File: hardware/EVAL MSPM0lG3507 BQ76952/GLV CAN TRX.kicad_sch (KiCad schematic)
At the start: 11 parts, among them U10 MCP2542FDxMF, U5 ISO7721D, U8 L78L05_SOT89

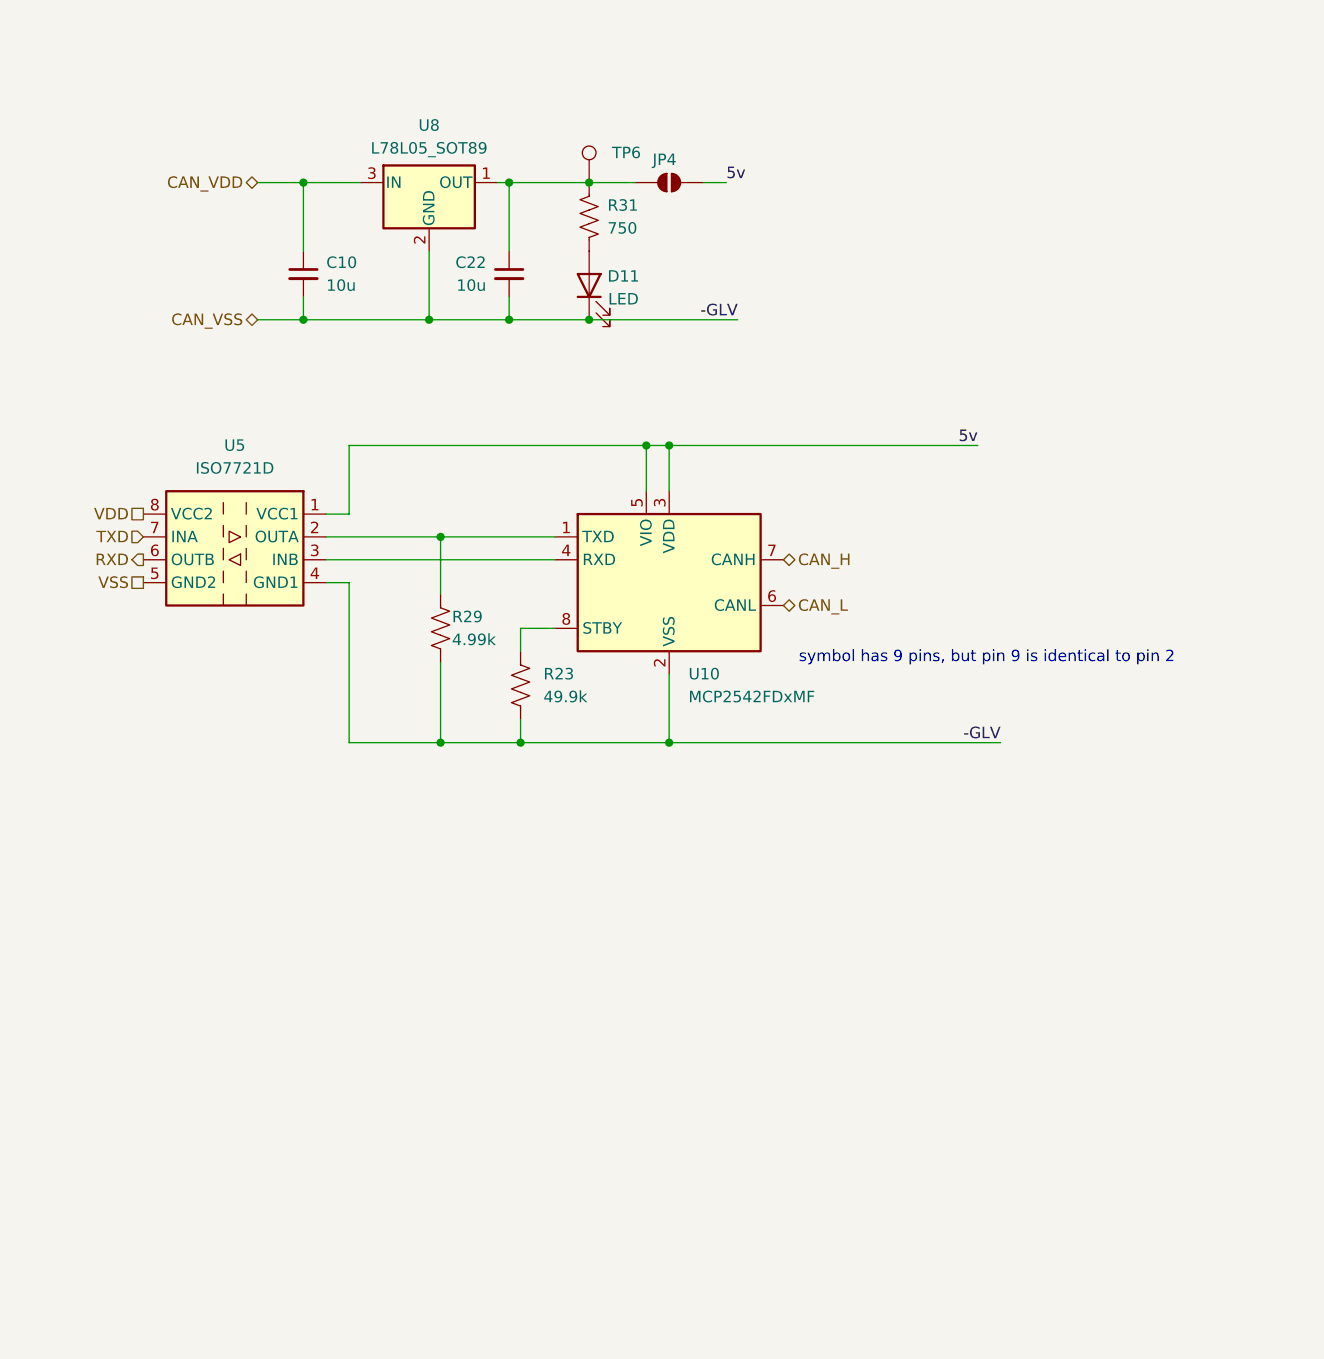
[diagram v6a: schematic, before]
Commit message: reordered can sub section
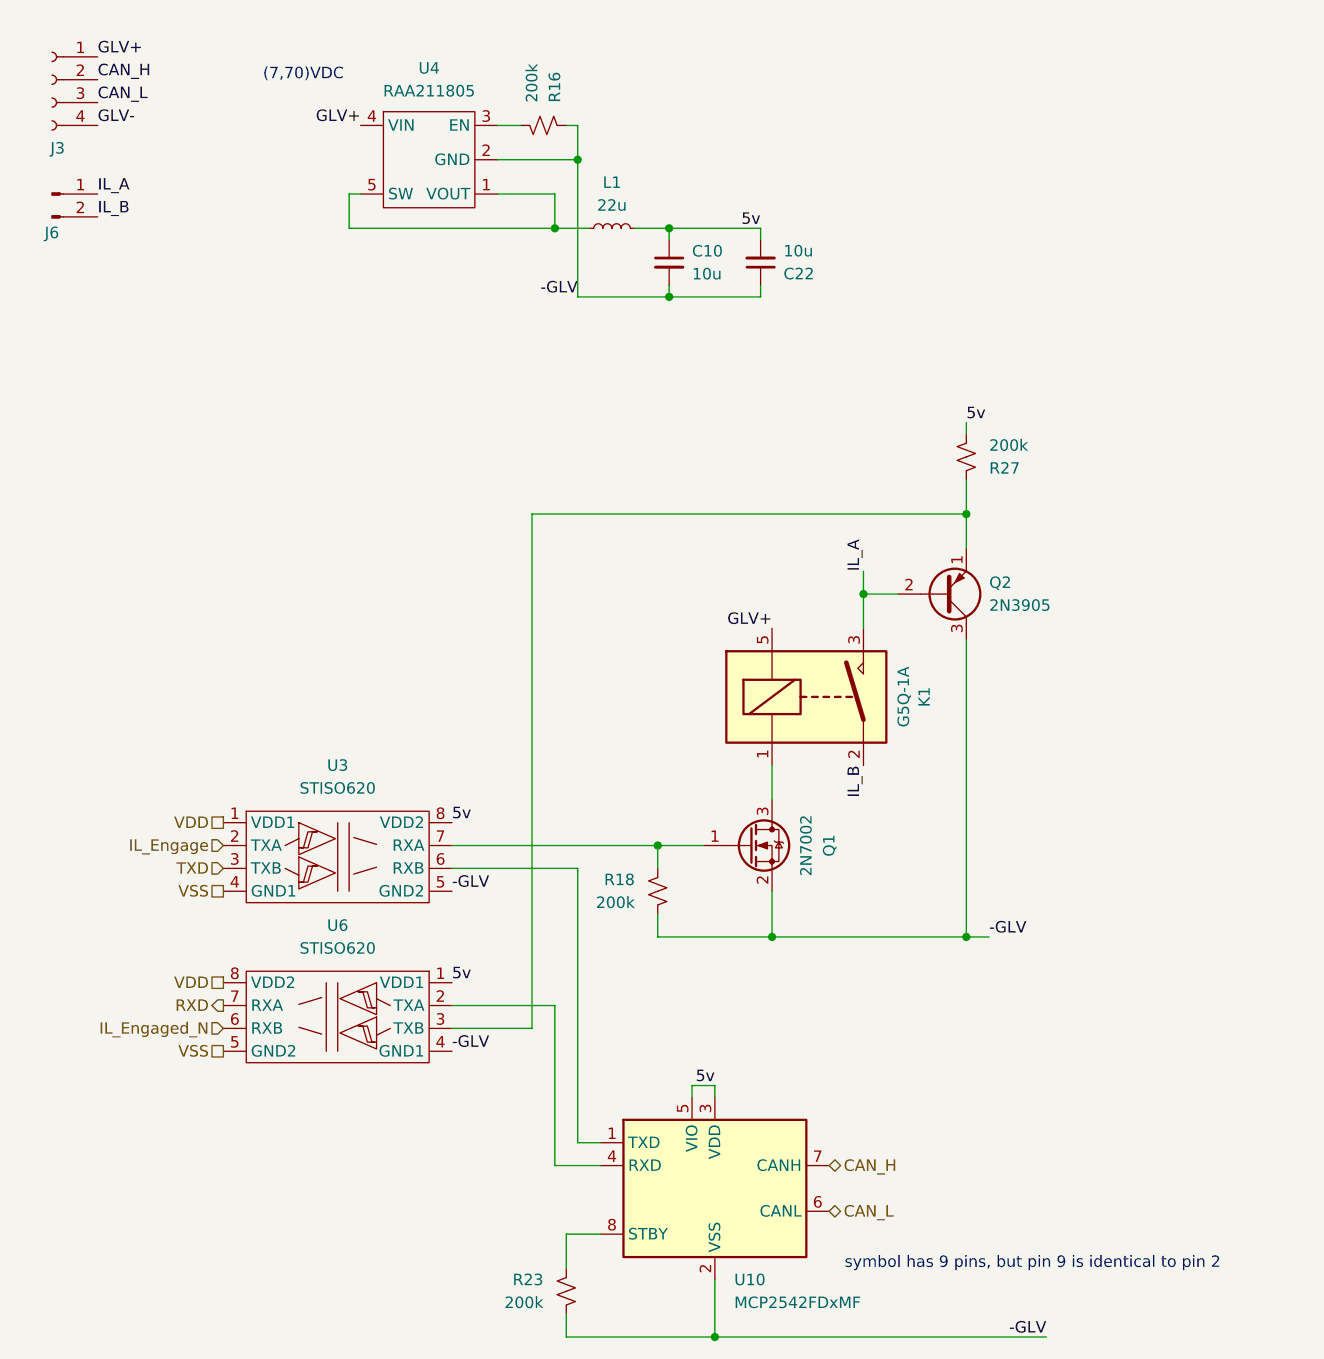
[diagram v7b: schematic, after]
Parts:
- removed D11: LED, LED_SMD:LED_0603_1608Metric, symbol Device:LED
- removed JP4: SolderJumper_2_Open, Jumper:SolderJumper-2_P1.3mm_Open_TrianglePad1.0x1.5mm, symbol Jumper:SolderJumper_2_Open
- removed R23: 49.9k, Resistor_SMD:R_1206_3216Metric_Pad1.30x1.75mm_HandSolder, symbol Device:R_US
- removed R29: 4.99k, Resistor_SMD:R_1206_3216Metric_Pad1.30x1.75mm_HandSolder, symbol Device:R_US
- removed R31: 750, Resistor_SMD:R_1206_3216Metric_Pad1.30x1.75mm_HandSolder, symbol Device:R_US
- removed TP6: TestPoint, TestPoint:TestPoint_Loop_D2.50mm_Drill1.0mm_LowProfile, symbol Connector:TestPoint
- removed U5: ISO7721D, Package_SO:SOIC-8_3.9x4.9mm_P1.27mm, symbol Isolator:ISO7721D
- removed U8: L78L05_SOT89, Package_TO_SOT_SMD:SOT-89-3, symbol Regulator_Linear:L78L05_SOT89
- added J3: Conn_01x04_Socket, symbol Connector:Conn_01x04_Socket
- added J6: Conn_01x02_Pin, symbol Connector:Conn_01x02_Pin
- added K1: G5Q-1A, Relay_THT:Relay_SPST_Omron-G5Q-1A, symbol Relay:G5Q-1A
- added L1: 22u, Inductor_SMD:L_1210_3225Metric_Pad1.42x2.65mm_HandSolder, symbol Device:L_Small
- added Q1: 2N7002, Package_TO_SOT_SMD:SOT-23, symbol Transistor_FET:2N7002
- added Q2: 2N3905, Package_TO_SOT_THT:TO-92_Inline, symbol Transistor_BJT:2N3905
- added R16, R18, R23, R27: 200k, Resistor_SMD:R_0805_2012Metric_Pad1.20x1.40mm_HandSolder, symbol Device:R_Small_US
- added U3, U6: STISO620, Package_SO:SOIC-8_3.9x4.9mm_P1.27mm, symbol zzLocalLibrary:STISO620TR
- added U4: RAA211805, Package_TO_SOT_SMD:TSOT-23-5, symbol zzLocalLibrary:RAA211805
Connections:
- net CAN_VDD is gone; now on net 5v: C10.1
- net 5v: now also C22.2, L1.2, R27.1, U3.8 (VDD2), U6.1 (VDD1)
- net CAN_H: now also J3.2 (Pin_2)
- net CAN_L: now also J3.3 (Pin_3)
- net RXD: now also U6.7 (RXA)
- net TXD: now also U3.3 (TXB)
- net VDD: now also U3.1 (VDD1), U6.8 (VDD2)
- net VSS: now also U3.4 (GND1), U6.5 (GND2)
- net at U10.1 (TXD): now also U3.6 (RXB)
- net at U10.4 (RXD): now also U6.2 (TXA)
- net at U10.8 (STBY): now also R23.2
- net -GLV: now reaches C22.1
- net -GLV: now also C10.2, U10.2 (VSS), U10.9 (VSS), Q1.2 (S), Q2.3 (C), R16.2, R18.1, R23.1, U3.5 (GND2), U4.2 (GND), U6.4 (GND1)
- removed net CAN_VSS: C10.2, C22.2, U10.2 (VSS), U10.9 (VSS)
- new net: K1.1, Q1.3 (D)
- new net: Q1.1 (G), R18.2, U3.7 (RXA)
- new net: Q2.1 (E), R27.2, U6.3 (TXB)
- new net: L1.1, U4.1 (VOUT), U4.5 (SW)
- new net: R16.1, U4.3 (EN)
- new net GLV+: J3.1 (Pin_1), K1.5, U4.4 (VIN)
- new net GLV-: J3.4 (Pin_4)
- new net IL_A: J6.1 (Pin_1), K1.3, Q2.2 (B)
- new net IL_B: J6.2 (Pin_2), K1.2
- new net IL_Engage: U3.2 (TXA)
- new net IL_Engaged_N: U6.6 (RXB)
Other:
- note added: "(7,70)VDC"
- moved on the sheet: C10, C22, U10

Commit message: aec
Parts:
- removed Q1: 2N7002, Package_TO_SOT_SMD:SOT-23, symbol Transistor_FET:2N7002
- added C6: 10u, Capacitor_SMD:C_1206_3216Metric_Pad1.33x1.80mm_HandSolder, symbol Device:C_Small
- added D2: ES1D, Diode_SMD:D_SMA, symbol Device:D_Schottky_Small
- added U5: FDMS8333L, zzLocalLibraries-Footprints:Power 56, symbol zzLocalLibrary:FDMS8333L
- J3: footprint (none) -> Connector_PinHeader_2.54mm:PinHeader_1x04_P2.54mm_Vertical
- J6: footprint (none) -> Connector_PinHeader_2.54mm:PinHeader_1x02_P2.54mm_Vertical
- U10: footprint zzLocalLibraries-Footprints:SOIC-8_4.9x6.0mm_P1.27mm -> Package_SO:JEITA_SOIC-8_3.9x4.9mm_P1.27mm
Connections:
- net -GLV: now also C22.2, C6.2, D2.2 (A), U5.1 (S); no longer C22.1, R16.2
- net 5v: now also C22.1, U4.1 (VOUT); no longer C22.2
- net GLV+: now also R16.2, C6.1
- net at K1.1: now also U5.3 (D)
- net at R18.2, U3.7 (RXA): now also U5.2 (G)
- net at L1.1, U4.5 (SW): now also D2.1 (K); no longer U4.1 (VOUT)
- net IL_Engaged_N renamed IL_Presense
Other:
- note added: "galvanic isolation required by FSAE rules. symbol shows capaciative, symbol is wrong"
- moved on the sheet: C10, C22, K1, L1, Q2, R27
